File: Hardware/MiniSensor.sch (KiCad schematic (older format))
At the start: 27 parts, among them CON1 AVR-ISP-6, IC1 ATMEGA328P-A, P1 Boost Converter Module, P2 CONN_01X06, P3 CONN_01X06, P4 CONN_01X06, U1 AMS1117, U2 AT25DF512C, U3 NRF24L01, U4 ATSHA204A

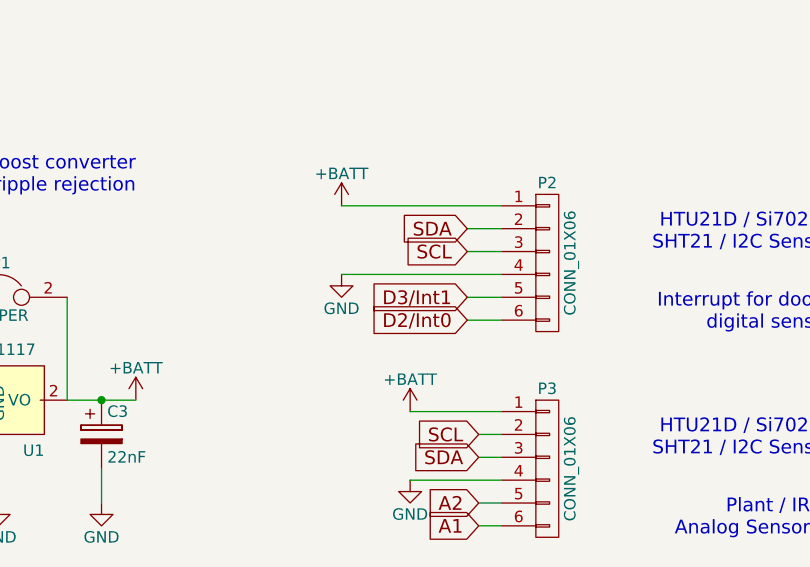
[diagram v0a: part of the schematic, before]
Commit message: schematics updated to final version 1, gerber export added
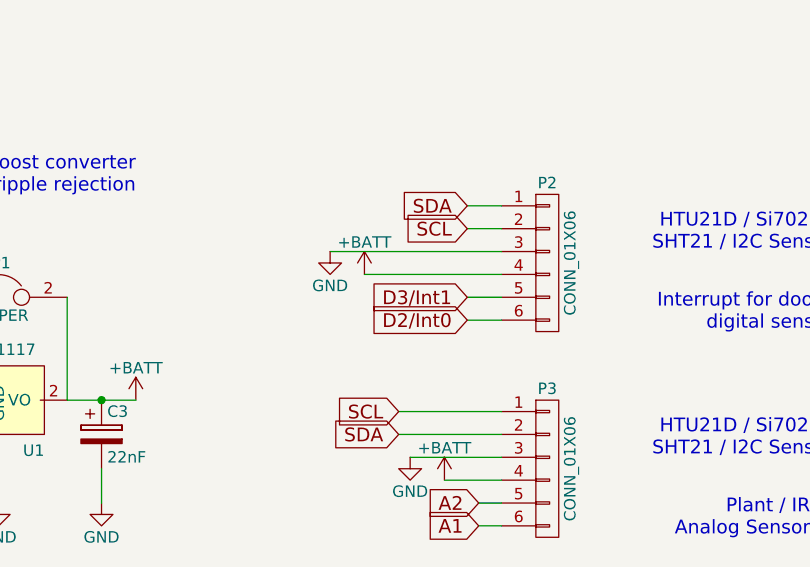
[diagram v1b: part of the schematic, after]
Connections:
- net +BATT: now also P2.4 (P4), P3.4 (P4); no longer P2.1 (P1), P3.1 (P1)
- net GND: now also P2.3 (P3), P3.3 (P3); no longer P2.4 (P4), P3.4 (P4)
- net SCL: now also P2.2 (P2), P3.1 (P1); no longer P2.3 (P3), P3.2 (P2)
- net SDA: now also P2.1 (P1), P3.2 (P2); no longer P2.2 (P2), P3.3 (P3)
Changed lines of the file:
@@
 L GND #PWR011
 U 1 1 573519DC
-P 4050 6650
-F 0 "#PWR011" H 4050 6400 50  0001 C CNN
-F 1 "GND" H 4050 6500 50  0000 C CNN
-F 2 "" H 4050 6650 50  0000 C CNN
-F 3 "" H 4050 6650 50  0000 C CNN
-	1    4050 6650
+P 4050 6550
+F 0 "#PWR011" H 4050 6300 50  0001 C CNN
+F 1 "GND" H 4050 6400 50  0000 C CNN
+F 2 "" H 4050 6550 50  0000 C CNN
+F 3 "" H 4050 6550 50  0000 C CNN
+	1    4050 6550
 	1    0    0    -1
 $EndComp
@@
 L +BATT #PWR019
 U 1 1 57532FE1
-P 4050 6350
-F 0 "#PWR019" H 4050 6200 50  0001 C CNN
-F 1 "+BATT" H 4050 6490 50  0000 C CNN
-F 2 "" H 4050 6350 50  0000 C CNN
-F 3 "" H 4050 6350 50  0000 C CNN
-	1    4050 6350
+P 4200 6650
+F 0 "#PWR019" H 4200 6500 50  0001 C CNN
+F 1 "+BATT" H 4200 6790 50  0000 C CNN
+F 2 "" H 4200 6650 50  0000 C CNN
+F 3 "" H 4200 6650 50  0000 C CNN
+	1    4200 6650
 	1    0    0    -1
 $EndComp
@@
 L +BATT #PWR020
 U 1 1 5753339F
-P 3750 5450
-F 0 "#PWR020" H 3750 5300 50  0001 C CNN
-F 1 "+BATT" H 3750 5590 50  0000 C CNN
-F 2 "" H 3750 5450 50  0000 C CNN
-F 3 "" H 3750 5450 50  0000 C CNN
-	1    3750 5450
+P 3850 5750
+F 0 "#PWR020" H 3850 5600 50  0001 C CNN
+F 1 "+BATT" H 3850 5890 50  0000 C CNN
+F 2 "" H 3850 5750 50  0000 C CNN
+F 3 "" H 3850 5750 50  0000 C CNN
+	1    3850 5750
 	1    0    0    -1
 $EndComp
@@
 L GND #PWR021
 U 1 1 575333E6
-P 3750 5750
-F 0 "#PWR021" H 3750 5500 50  0001 C CNN
-F 1 "GND" H 3750 5600 50  0000 C CNN
-F 2 "" H 3750 5750 50  0000 C CNN
-F 3 "" H 3750 5750 50  0000 C CNN
-	1    3750 5750
-	1    0    0    -1
-$EndComp
-Text GLabel 4350 6450 0    60   Input ~ 0
+P 3700 5650
+F 0 "#PWR021" H 3700 5400 50  0001 C CNN
+F 1 "GND" H 3700 5500 50  0000 C CNN
+F 2 "" H 3700 5650 50  0000 C CNN
+F 3 "" H 3700 5650 50  0000 C CNN
+	1    3700 5650
+	1    0    0    -1
+$EndComp
+Text GLabel 4000 6350 0    60   Input ~ 0
 SCL
+Text GLabel 4300 5450 0    60   Input ~ 0
+SDA
 Text GLabel 4300 5550 0    60   Input ~ 0
-SDA
-Text GLabel 4300 5650 0    60   Input ~ 0
 SCL
-Text GLabel 4350 6550 0    60   Input ~ 0
+Text GLabel 4000 6450 0    60   Input ~ 0
 SDA
 Wire Wire Line
@@
 	4350 6750 4450 6750
 Wire Wire Line
-	4450 6650 4050 6650
-Wire Wire Line
-	4350 6550 4450 6550
-Wire Wire Line
-	4450 6450 4350 6450
-Wire Wire Line
-	4450 6350 4050 6350
-Wire Wire Line
 	4450 5950 4300 5950
 Wire Wire Line
 	4300 5850 4450 5850
-Wire Wire Line
-	4450 5750 3750 5750
-Wire Wire Line
-	4300 5650 4450 5650
-Wire Wire Line
-	4450 5550 4300 5550
-Wire Wire Line
-	4450 5450 3750 5450
 Text Notes 5900 6550 2    60   ~ 0
 HTU21D / Si7021 / \nSHT21 / I2C Sensor
@@
 	1    0    0    -1
 $EndComp
+Wire Wire Line
+	4200 6650 4450 6650
+Wire Wire Line
+	4450 6550 4050 6550
+Wire Wire Line
+	4000 6450 4450 6450
+Wire Wire Line
+	4450 6350 4000 6350
+Wire Wire Line
+	4450 5550 4300 5550
+Wire Wire Line
+	4300 5450 4450 5450
+Wire Wire Line
+	4450 5650 3700 5650
+Wire Wire Line
+	3850 5750 4450 5750
 $EndSCHEMATC
